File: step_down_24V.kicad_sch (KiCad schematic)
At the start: 19 parts

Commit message: Primer sesion de ruteo
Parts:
- gave numbers to parts that had none: 4
- renumbered C12 to C11, C13 to C12, C11 to C13, C15 to C14, C14 to C15, R9 to R10, R4 to R11, R3 to R5, R5 to R6, R6 to R7, R7 to R9
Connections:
- net GND: now also U2.9 (EP)

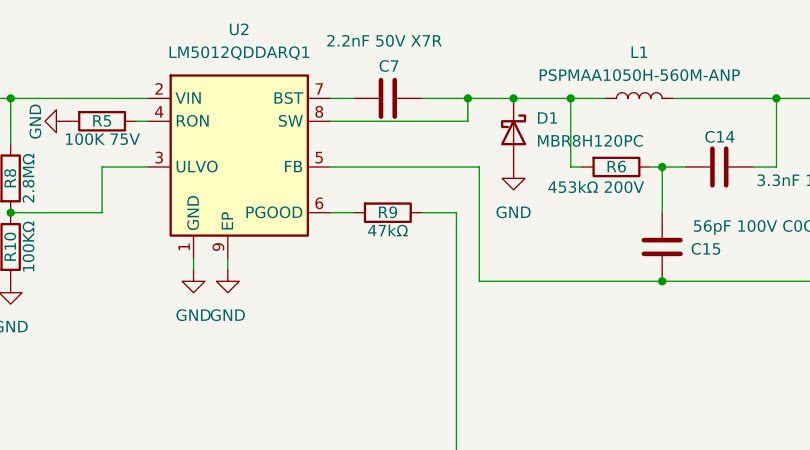
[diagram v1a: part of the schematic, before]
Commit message: Agregado los testpoint, falta leds indicadores y serigrafia y cerramos
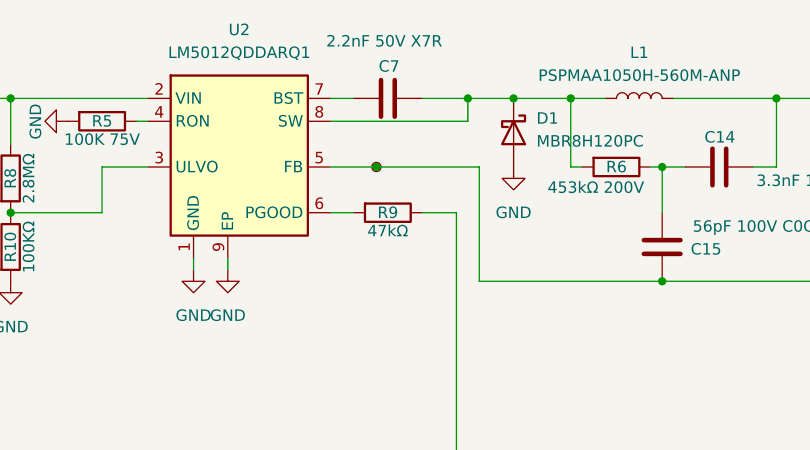
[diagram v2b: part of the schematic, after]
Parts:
- added TP25: FB_24V, 0_ZA_Lib:TestPoint_Pad_D2.0mm_silk_value, symbol Connector:TestPoint_Small
- U2: footprint Package_SO:SOIC-8-1EP_3.9x4.9mm_P1.27mm_EP2.95x4.9mm_Mask2.71x3.4mm_ThermalVias -> 0_ZA_Lib:SOIC-8-1EP_3.9x4.9mm_P1.27mm_EP2.95x4.9mm_Mask2.71x3.4mm_ThermalVias
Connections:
- net at C15.2, R11.2, R7.1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: now also TP25.1
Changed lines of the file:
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@@
 	)
 	(junction
+		(at 140.97 80.01)
+		(diameter 0)
+		(color 0 0 0 0)
+	)
+	(junction
 		(at 91.44 72.39)
 		(diameter 0)
@@
 	(wire
 		(pts
+			(xy 140.97 80.01) (xy 152.4 80.01)
+		)
+		(stroke
+			(width 0)
+			(type default)
+		)
+	)
+	(wire
+		(pts
 			(xy 115.57 80.01) (xy 110.49 80.01)
 		)
@@
 	(wire
 		(pts
-			(xy 135.89 80.01) (xy 152.4 80.01)
+			(xy 135.89 80.01) (xy 140.97 80.01)
 		)
 		(stroke
@@
 	)
 	(symbol
+		(lib_id "Connector:TestPoint_Small")
+		(at 140.97 80.01 0)
+		(unit 1)
+		(exclude_from_sim no)
+		(in_bom yes)
+		(on_board yes)
+		(dnp no)
+		(property "Reference" "TP25"
+			(at 142.24 78.7399 0)
+			(effects
+				(font
+					(size 1.27 1.27)
+				)
+				(justify left)
+				(hide yes)
+			)
+		)
+		(property "Value" "FB_24V"
+			(at 154.432 78.994 0)
+			(effects
+				(font
+					(size 1.27 1.27)
+				)
+				(justify left)
+				(hide yes)
+			)
+		)
+		(property "Footprint" "0_ZA_Lib:TestPoint_Pad_D2.0mm_silk_value"
+			(at 146.05 80.01 0)
+			(effects
+				(font
+					(size 1.27 1.27)
+				)
+				(hide yes)
+			)
+		)
+		(property "Datasheet" "~"
+			(at 146.05 80.01 0)
+			(effects
+				(font
+					(size 1.27 1.27)
+				)
+				(hide yes)
+			)
+		)
+		(property "Description" "test point"
+			(at 140.97 80.01 0)
+			(effects
+				(font
+					(size 1.27 1.27)
+				)
+				(hide yes)
+			)
+		)
+		(pin "1"
+		)
+		(instances
+			(project "pdb"
+				(path "/402e9eb5-eedc-44fb-9e44-3f0a74044b6b/4ac74e48-daea-4f94-9ecb-ed9b659863ee"
+					(reference "TP25")
+					(unit 1)
+				)
+			)
+		)
+	)
+	(symbol
 		(lib_id "power:GND")
 		(at 203.2 107.95 0)
@@
 			)
 		)
-		(property "Footprint" "Package_SO:SOIC-8-1EP_3.9x4.9mm_P1.27mm_EP2.95x4.9mm_Mask2.71x3.4mm_ThermalVias"
+		(property "Footprint" "0_ZA_Lib:SOIC-8-1EP_3.9x4.9mm_P1.27mm_EP2.95x4.9mm_Mask2.71x3.4mm_ThermalVias"
 			(at 127 88.9 0)
 			(effects
